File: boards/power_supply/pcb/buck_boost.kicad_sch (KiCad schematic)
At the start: 37 parts

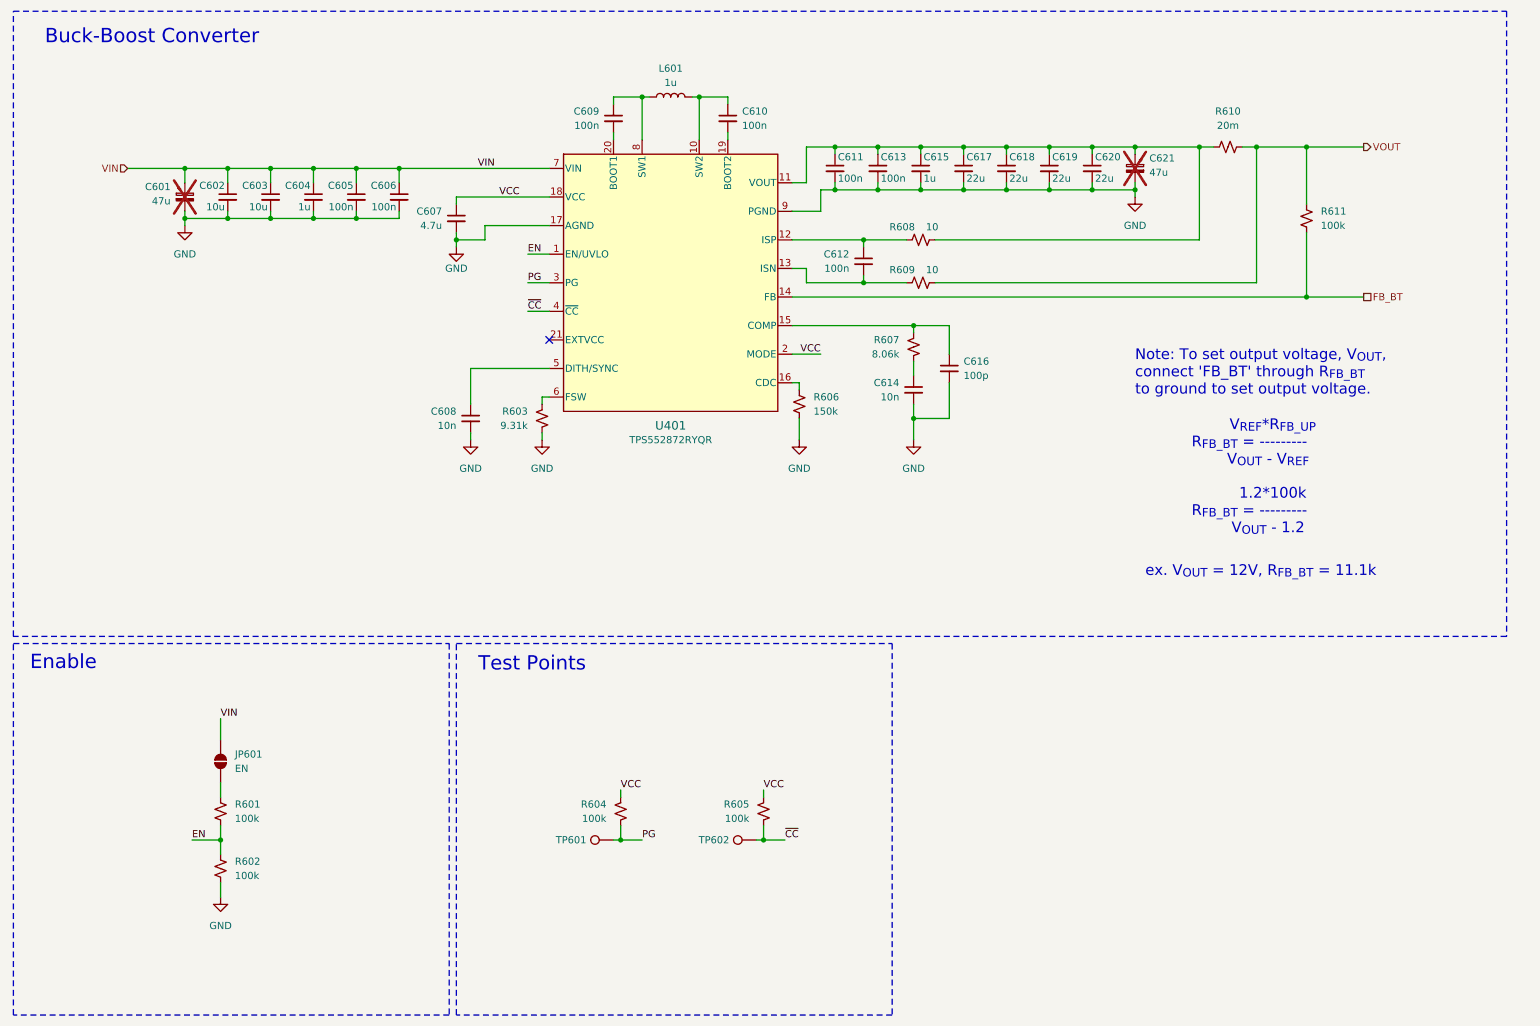
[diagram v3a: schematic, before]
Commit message: created psu footprints
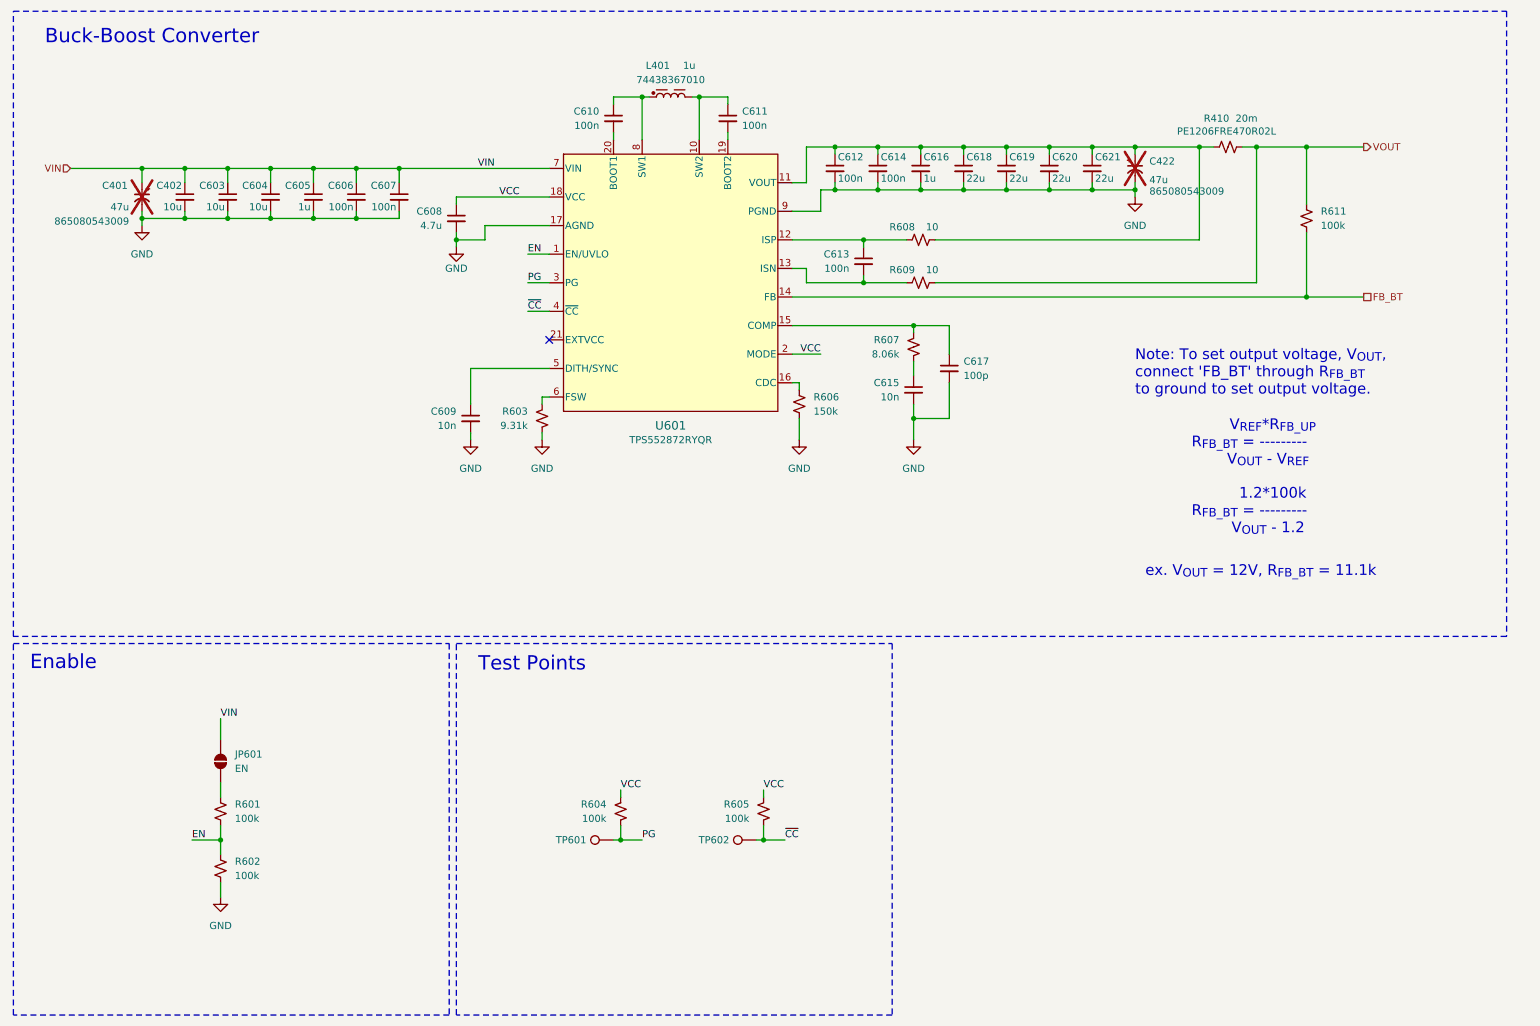
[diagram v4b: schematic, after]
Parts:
- removed C601, C621: 47u, symbol Device:C_Polarized_Small
- removed L601: 1u, symbol Device:L
- removed R610: 20m, symbol Device:R_Small_US
- added C401, C422: 47u, 865080543009:865080543009, symbol 865080543009:865080543009
- added C402: 10u, symbol Device:C_Small
- added L401: 1u, 74438367010:74438367010, symbol 74438367010:74438367010
- added R410: 20m, PE1206FRE470R02L:PE1206FRE470R02L, symbol PE1206FRE470R02L:PE1206FRE470R02L
- renumbered C602 to C603, C603 to C604, C604 to C605, C605 to C606, C606 to C607, C607 to C608, C608 to C609, C609 to C610, C610 to C611, C611 to C612, C612 to C613, C613 to C614, C614 to C615, C615 to C616, C616 to C617, C617 to C618, C618 to C619, C619 to C620, C620 to C621, U401 to U601
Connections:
- net GND: now also C401.1, C402.2, C422.1
- net VIN: now also C401.1, C402.1
- net VOUT: now also R410.2
- net at C612.1, C614.1, C616.1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: now also C422.1, R410.1
- net at C611.1, U601.10 (SW2): now also L401.2
- net at C610.1, U601.8 (SW1): now also L401.1

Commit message: starting psu layout
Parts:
- removed C401, C422: 47u, 865080543009:865080543009, symbol 865080543009:865080543009
- added C601, C622: 47u, 865080543009:865080543009, symbol 865080543009:865080543009
- C602: renamed from C402; footprint (none) -> Capacitor_SMD:C_0805_2012Metric
- C603, C604, C608: footprint (none) -> Capacitor_SMD:C_0805_2012Metric
- C605, C606, C607, C609, C610, C611, C612, C613, C614, C615, C616, C617: footprint (none) -> Capacitor_SMD:C_0603_1608Metric
- C618, C619, C620, C621: footprint (none) -> Capacitor_SMD:C_1206_3216Metric
- JP601: footprint (none) -> Jumper:SolderJumper-2_P1.3mm_Open_RoundedPad1.0x1.5mm
- R601, R602, R603, R604, R605, R606, R607, R608, R609, R611: footprint (none) -> Resistor_SMD:R_0603_1608Metric
- TP601, TP602: footprint (none) -> TestPoint:TestPoint_Pad_D1.0mm
- U601: footprint VQFN21_RYQ_TEX -> TPS552872RYQR:TPS552872RYQR
- renumbered L401 to L601, R410 to R610
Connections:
- net GND: now also C601.2, C622.2
- net VIN: now also C601.1
- net at C612.1, C614.1, C616.1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: now also C622.1
